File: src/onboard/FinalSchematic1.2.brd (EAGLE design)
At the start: 137.6 x 80 mm, 85 parts, among them IC1 MIC29310-5.0BT, IC3 A5975D

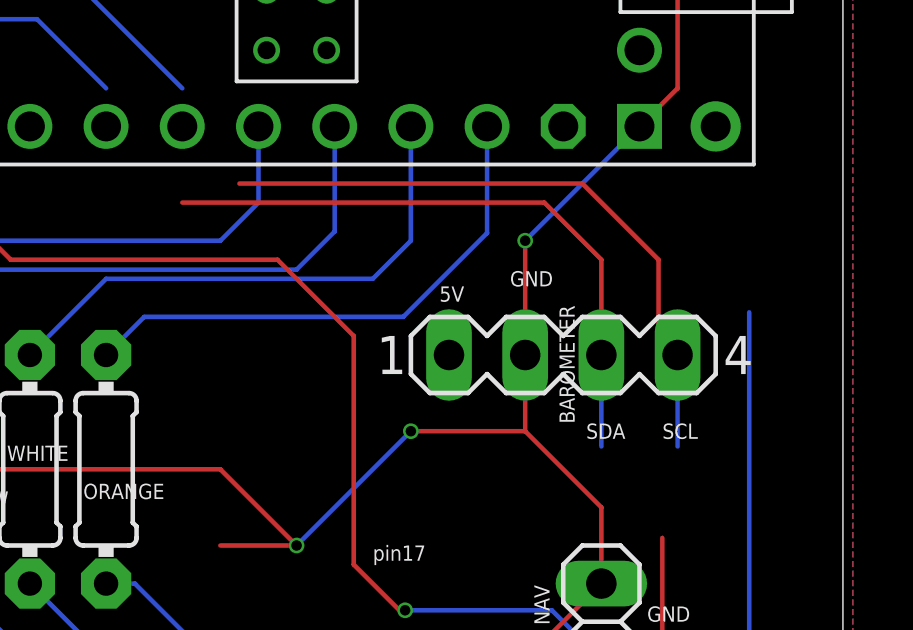
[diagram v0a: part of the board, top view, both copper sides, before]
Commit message: Removed old baro
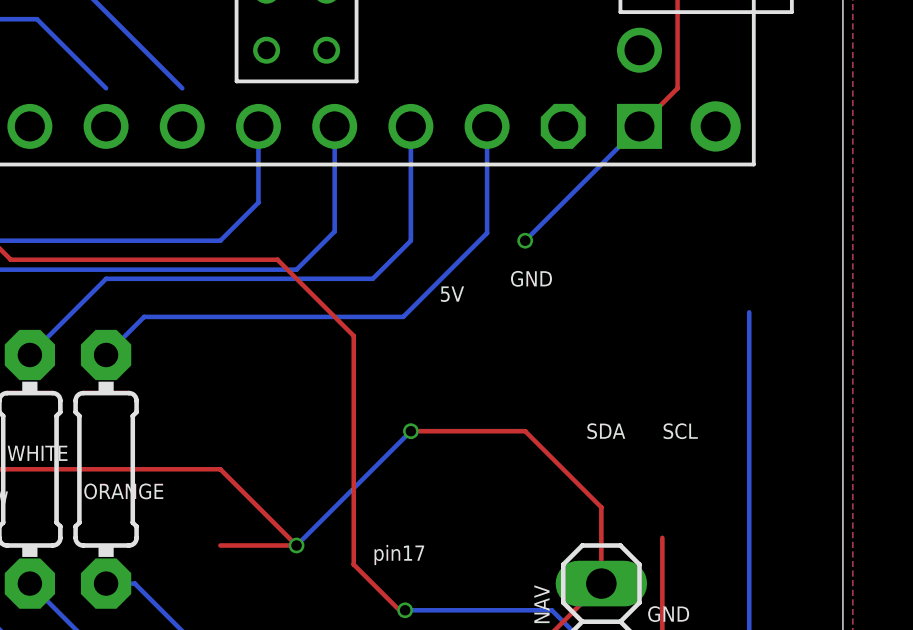
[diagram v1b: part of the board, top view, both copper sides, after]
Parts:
- removed BAROMETER: (no value), con-lstb:MA04-1
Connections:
- net 5V: no longer BAROMETER.1
- net GND: no longer BAROMETER.2
- net SCL: no longer BAROMETER.4
- net SDA: no longer BAROMETER.3
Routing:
- net SCL: track 141.5 -> 120.0 mm
- net SDA: track 130.1 -> 109.1 mm
- net GND: track 373.3 -> 366.9 mm
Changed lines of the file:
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@@
 </autorouter>
 <elements>
-<element name="BAROMETER" library="con-lstb" library_urn="urn:adsk.eagle:library:162" package="MA04-1" package3d_urn="urn:adsk.eagle:package:8337/1" value="" x="92.71" y="26.67" smashed="yes">
-<attribute name="MF" value="" x="125.73" y="-57.15" size="1.778" layer="27" display="off"/>
-<attribute name="MPN" value="" x="125.73" y="-57.15" size="1.778" layer="27" display="off"/>
-<attribute name="NAME" x="93.091" y="24.384" size="0.508" layer="25" ratio="10" rot="R90"/>
-<attribute name="OC_FARNELL" value="unknown" x="125.73" y="-57.15" size="1.778" layer="27" display="off"/>
-<attribute name="OC_NEWARK" value="unknown" x="125.73" y="-57.15" size="1.778" layer="27" display="off"/>
-<attribute name="POPULARITY" value="41" x="125.73" y="-57.15" size="1.778" layer="27" display="off"/>
-<attribute name="VALUE" x="93.345" y="28.321" size="1.27" layer="27" ratio="10"/>
-</element>
 <element name="BLUE" library="adafruit" library_urn="urn:adsk.eagle:library:420" package="0204/7" package3d_urn="urn:adsk.eagle:package:6240596/1" value="80" x="53.34" y="27.94" smashed="yes" rot="R270">
 <attribute name="NAME" x="52.832" y="26.9494" size="0.508" layer="25" ratio="12"/>
@@
 <contactref element="C10" pad="1"/>
 <contactref element="GREEN" pad="1"/>
-<contactref element="BAROMETER" pad="1"/>
 <contactref element="TEENSY4.1" pad="VIN"/>
 <contactref element="RADIO" pad="1"/>
@@
 <contactref element="C2" pad="1"/>
 <wire x1="97.79" y1="34.29" x2="88.9" y2="73.66" width="0" layer="19" extent="1-1"/>
-<wire x1="88.9" y1="26.67" x2="97.79" y2="34.29" width="0" layer="19" extent="1-1"/>
-<wire x1="68.58" y1="16.51" x2="88.9" y2="26.67" width="0" layer="19" extent="1-1"/>
+<wire x1="68.58" y1="16.51" x2="97.79" y2="34.29" width="0" layer="19" extent="1-1"/>
 <wire x1="64.77" y1="10.795" x2="68.58" y2="16.51" width="0" layer="19" extent="1-1"/>
 <wire x1="54.61" y1="19.05" x2="64.77" y2="10.795" width="0" layer="19" extent="1-1"/>
@@
 <contactref element="SERVO_DRIVER" pad="27"/>
 <contactref element="IMU" pad="SDA"/>
-<contactref element="BAROMETER" pad="3"/>
-<wire x1="93.98" y1="23.622" x2="93.98" y2="26.67" width="0.1524" layer="16"/>
 <wire x1="34.627" y1="39.156" x2="48.474" y2="39.156" width="0.1524" layer="16"/>
 <wire x1="48.474" y1="39.156" x2="49.7666" y2="37.8634" width="0.1524" layer="16"/>
@@
 <wire x1="49.7666" y1="37.8634" x2="75.1666" y2="37.8634" width="0.1524" layer="16"/>
 <contactref element="NAV" pad="3"/>
-<wire x1="93.98" y1="29.845" x2="93.98" y2="26.67" width="0.1524" layer="1"/>
 <wire x1="97.155" y1="13.97" x2="93.98" y2="13.97" width="0.1524" layer="16"/>
 <wire x1="97.79" y1="14.605" x2="97.155" y2="13.97" width="0.1524" layer="16"/>
@@
 <wire x1="33.143" y1="40.64" x2="34.627" y2="39.156" width="0.1524" layer="1"/>
 <via x="-10.16" y="40.64" extent="1-16" drill="0.35"/>
-<wire x1="93.98" y1="29.845" x2="92.075" y2="31.75" width="0.1524" layer="1"/>
-<wire x1="92.075" y1="31.75" x2="80.01" y2="31.75" width="0.1524" layer="1"/>
 <contactref element="TEENSY4.1" pad="18-A4/SDA0"/>
 <contactref element="R33" pad="1"/>
 <contactref element="TP2" pad="TP"/>
-<wire x1="77.47" y1="34.29" x2="80.01" y2="31.75" width="0" layer="19" extent="1-1"/>
 <wire x1="77.47" y1="35.56" x2="77.47" y2="34.29" width="0" layer="19" extent="16-16"/>
 <wire x1="-12.7" y1="38.1" x2="-10.16" y2="40.64" width="0" layer="19" extent="1-1"/>
-<wire x1="93.98" y1="13.97" x2="93.98" y2="23.622" width="0" layer="19" extent="16-16"/>
+<wire x1="93.98" y1="13.97" x2="77.47" y2="34.29" width="0" layer="19" extent="1-1"/>
 <wire x1="-34.544" y1="-70.612" x2="-24.365" y2="38.972" width="0" layer="19" extent="1-1"/>
 </signal>
@@
 <contactref element="SERVO_DRIVER" pad="26"/>
 <contactref element="IMU" pad="SCL"/>
-<contactref element="BAROMETER" pad="4"/>
 <wire x1="80.01" y1="35.56" x2="74.93" y2="40.64" width="0.1524" layer="16"/>
-<wire x1="96.52" y1="26.67" x2="96.52" y2="23.622" width="0.1524" layer="16"/>
 <wire x1="34.827" y1="41.656" x2="48.514" y2="41.656" width="0.1524" layer="16"/>
 <wire x1="48.514" y1="41.656" x2="49.53" y2="40.64" width="0.1524" layer="16"/>
@@
 <wire x1="32.287" y1="41.656" x2="32.033" y2="41.91" width="0.1524" layer="1"/>
 <wire x1="-12.7" y1="41.91" x2="32.033" y2="41.91" width="0.1524" layer="1"/>
-<wire x1="96.52" y1="26.67" x2="95.885" y2="27.305" width="0.1524" layer="1"/>
-<wire x1="95.885" y1="27.305" x2="95.885" y2="29.845" width="0.1524" layer="1"/>
-<wire x1="95.885" y1="29.845" x2="93.345" y2="32.385" width="0.1524" layer="1"/>
-<wire x1="93.345" y1="32.385" x2="81.915" y2="32.385" width="0.1524" layer="1"/>
 <contactref element="TEENSY4.1" pad="19-A5/SCL0"/>
 <contactref element="R32" pad="1"/>
 <contactref element="TP3" pad="TP"/>
-<wire x1="80.01" y1="34.29" x2="81.915" y2="32.385" width="0" layer="19" extent="1-1"/>
 <wire x1="80.01" y1="35.56" x2="80.01" y2="34.29" width="0" layer="19" extent="16-16"/>
-<wire x1="96.012" y1="20.574" x2="96.52" y2="23.622" width="0" layer="19" extent="1-16"/>
 <wire x1="-10.16" y1="45.72" x2="-12.7" y2="41.91" width="0" layer="19" extent="1-1"/>
+<wire x1="96.012" y1="20.574" x2="80.01" y2="34.29" width="0" layer="19" extent="1-1"/>
 <wire x1="-34.544" y1="-75.184" x2="-25.015" y2="38.972" width="0" layer="19" extent="1-1"/>
 </signal>
@@
 <contactref element="GPSMTK3339" pad="GND"/>
 <contactref element="RADIO" pad="2"/>
-<contactref element="BAROMETER" pad="2"/>
 <contactref element="SERVO_DRIVER" pad="25"/>
 <contactref element="C10" pad="2"/>
@@
 <contactref element="R53" pad="1"/>
 <contactref element="C12" pad="2"/>
-<wire x1="91.44" y1="26.67" x2="91.44" y2="30.48" width="0.1524" layer="1"/>
 <via x="91.44" y="30.48" extent="1-16" drill="0.35"/>
 <wire x1="95.25" y1="34.29" x2="91.44" y2="30.48" width="0.1524" layer="16"/>
@@
 <contactref element="NAV" pad="1"/>
 <wire x1="93.98" y1="21.59" x2="91.44" y2="24.13" width="0.1524" layer="1"/>
-<wire x1="91.44" y1="24.13" x2="91.44" y2="26.67" width="0.1524" layer="1"/>
 <wire x1="93.98" y1="21.59" x2="93.98" y2="19.05" width="0.1524" layer="1"/>
 <contactref element="C3" pad="2"/>
@@
 <wire x1="62.23" y1="34.29" x2="57.658" y2="29.464" width="0" layer="19" extent="1-1"/>
 <wire x1="76.2" y1="15.24" x2="81.28" y2="20.32" width="0" layer="19" extent="1-1"/>
+<wire x1="91.44" y1="30.48" x2="87.63" y2="24.13" width="0" layer="19" extent="1-1"/>
 <wire x1="52.07" y1="41.91" x2="62.23" y2="34.29" width="0" layer="19" extent="1-1"/>
 <wire x1="83.82" y1="46.53" x2="97.79" y2="49.53" width="0" layer="19" extent="1-1"/>

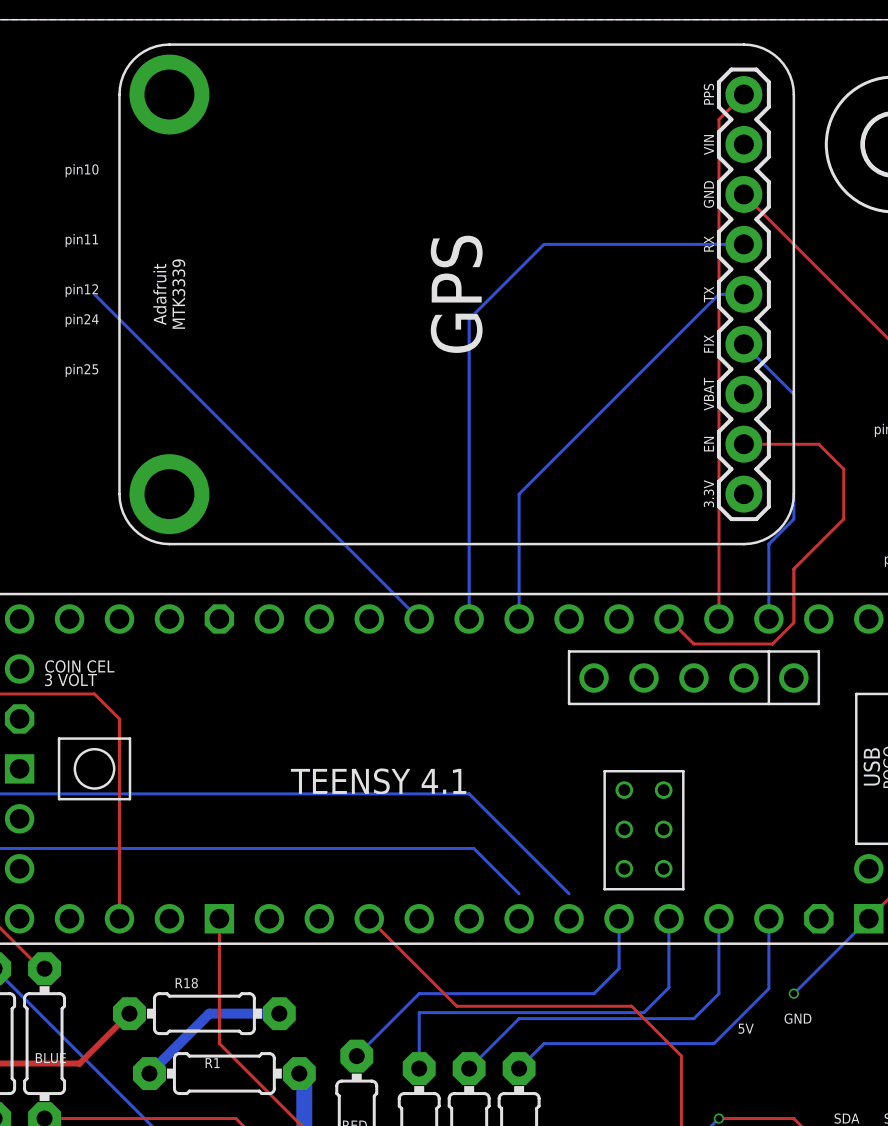
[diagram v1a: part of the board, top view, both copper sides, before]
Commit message: Rewired pins for easier routing
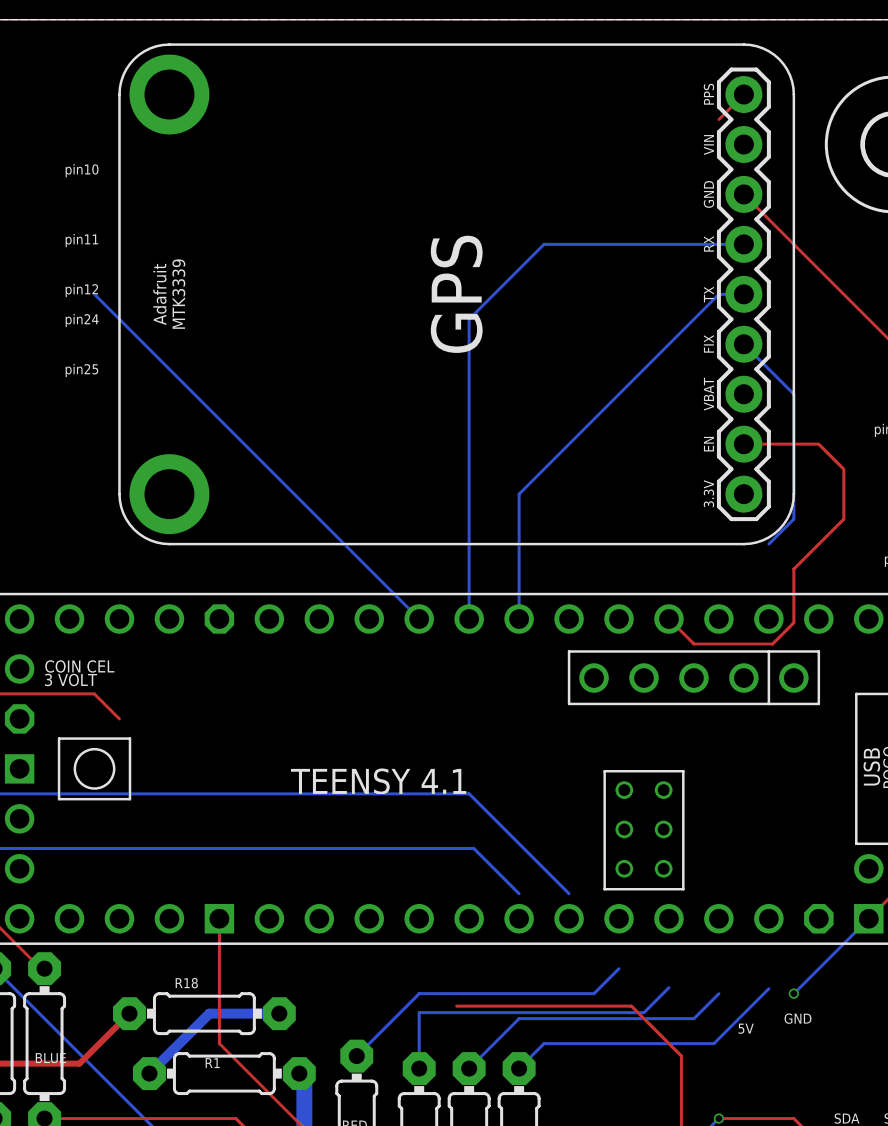
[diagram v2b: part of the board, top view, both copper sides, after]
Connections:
- net AUX_DATA: now also TEENSY4.1.6-OUT1D; no longer TEENSY4.1.9-OUT1C
- net BTN1: now also TEENSY4.1.14-A0/TX3/SPDIF_OUT
- net BTN2: now also TEENSY4.1.15-A1/RX3/SPDIF_IN
- net GPS_FIX: now also TEENSY4.1.3-LRCLK2; no longer TEENSY4.1.2-OUT2
- net GPS_PPS: now also TEENSY4.1.5-IN2; no longer TEENSY4.1.3-LRCLK2
- net IMU_INT: now also TEENSY4.1.22-A8/CTX1; no longer TEENSY4.1.40-A16/CS1
- net O_LED: now also TEENSY4.1.40-A16/CS1; no longer TEENSY4.1.23-A9/CRX1/MCLK1
- net RADIO_RST: now also TEENSY4.1.9-OUT1C; no longer TEENSY4.1.6-OUT1D
- net R_LED: now also TEENSY4.1.41-A17/MISO1; no longer TEENSY4.1.20-A6/TX5/LRCLK1
- net SELECT_PIN: now also TEENSY4.1.2-OUT2; no longer TEENSY4.1.15-A1/RX3/SPDIF_IN
- net W_LED: now also TEENSY4.1.38-A14/CS/IN1; no longer TEENSY4.1.22-A8/CTX1
- net Y_LED: now also TEENSY4.1.39-A15/CS/OUT1A; no longer TEENSY4.1.21-A7/RX5/BCLK1
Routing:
- net GPS_PPS: track 27.2 -> 1.80 mm
- net RADIO_RST: track 21.9 -> 45.2 mm
- net AUX_DATA: track 23.3 -> 0.00 mm
- net IMU_INT: track 33.9 -> 23.7 mm
- net SELECT_PIN: track 36.0 -> 29.7 mm
- net GPS_FIX: track 15.5 -> 11.7 mm
- net W_LED: track 18.1 -> 14.3 mm
- net O_LED: track 17.9 -> 14.4 mm
- net Y_LED: track 19.6 -> 16.1 mm
- net R_LED: track 17.7 -> 15.2 mm
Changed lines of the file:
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@@
 <signal name="GPS_FIX">
 <contactref element="GPSMTK3339" pad="FIX"/>
-<contactref element="TEENSY4.1" pad="2-OUT2"/>
 <wire x1="90.17" y1="53.34" x2="91.44" y2="54.61" width="0.1524" layer="16"/>
 <wire x1="91.44" y1="54.61" x2="91.44" y2="60.96" width="0.1524" layer="16"/>
 <wire x1="91.44" y1="60.96" x2="88.9" y2="63.5" width="0.1524" layer="16"/>
-<wire x1="90.17" y1="49.53" x2="90.17" y2="53.34" width="0.1524" layer="16"/>
+<contactref element="TEENSY4.1" pad="3-LRCLK2"/>
+<wire x1="87.63" y1="49.53" x2="90.17" y2="53.34" width="0" layer="19" extent="16-16"/>
 </signal>
 <signal name="GPS_PPS">
 <contactref element="GPSMTK3339" pad="PPS"/>
-<contactref element="TEENSY4.1" pad="3-LRCLK2"/>
-<wire x1="87.63" y1="49.53" x2="87.63" y2="74.93" width="0.1524" layer="1"/>
 <wire x1="87.63" y1="74.93" x2="88.9" y2="76.2" width="0.1524" layer="1"/>
+<contactref element="TEENSY4.1" pad="5-IN2"/>
+<wire x1="82.55" y1="49.53" x2="87.63" y2="74.93" width="0" layer="19" extent="1-1"/>
 </signal>
 <signal name="RADIO_EN">
@@
 <wire x1="44.45" y1="54.61" x2="44.45" y2="74.68" width="0.1524" layer="1"/>
 <wire x1="44.45" y1="74.68" x2="44.575" y2="74.805" width="0.1524" layer="1"/>
-<contactref element="TEENSY4.1" pad="6-OUT1D"/>
-<wire x1="44.45" y1="54.61" x2="80.01" y2="49.53" width="0" layer="19" extent="1-1"/>
+<contactref element="TEENSY4.1" pad="9-OUT1C"/>
+<wire x1="72.39" y1="49.53" x2="55.88" y2="66.04" width="0.1524" layer="16"/>
+<wire x1="45.72" y1="75.95" x2="55.88" y2="66.04" width="0" layer="19" extent="16-16"/>
 </signal>
 <signal name="RX2">
@@
 <signal name="IMU_INT">
 <contactref element="IMU" pad="INT"/>
-<contactref element="TEENSY4.1" pad="40-A16/CS1"/>
 <wire x1="36.191" y1="45.72" x2="34.627" y2="44.156" width="0.1524" layer="1"/>
 <wire x1="55.88" y1="45.72" x2="57.15" y2="44.45" width="0.1524" layer="1"/>
-<wire x1="57.15" y1="44.45" x2="57.15" y2="34.29" width="0.1524" layer="1"/>
 <wire x1="36.191" y1="45.72" x2="55.88" y2="45.72" width="0.1524" layer="1"/>
+<contactref element="TEENSY4.1" pad="22-A8/CTX1"/>
+<wire x1="57.15" y1="44.45" x2="87.63" y2="34.29" width="0" layer="19" extent="1-1"/>
 </signal>
 <signal name="RED">
@@
 <signal name="W_LED">
 <contactref element="WHITE" pad="1"/>
-<contactref element="TEENSY4.1" pad="22-A8/CTX1"/>
 <wire x1="87.63" y1="30.48" x2="86.36" y2="29.21" width="0.1524" layer="16"/>
-<wire x1="87.63" y1="30.48" x2="87.63" y2="34.29" width="0.1524" layer="16"/>
 <wire x1="77.47" y1="29.21" x2="74.93" y2="26.67" width="0.1524" layer="16"/>
 <wire x1="86.36" y1="29.21" x2="77.47" y2="29.21" width="0.1524" layer="16"/>
+<contactref element="TEENSY4.1" pad="38-A14/CS/IN1"/>
+<wire x1="52.07" y1="34.29" x2="74.93" y2="26.67" width="0" layer="19" extent="1-1"/>
 </signal>
 <signal name="Y_LED">
 <contactref element="YELLOW" pad="1"/>
-<contactref element="TEENSY4.1" pad="21-A7/RX5/BCLK1"/>
 <wire x1="85.09" y1="30.7848" x2="83.82" y2="29.5148" width="0.1524" layer="16"/>
-<wire x1="85.09" y1="30.7848" x2="85.09" y2="34.29" width="0.1524" layer="16"/>
 <wire x1="72.39" y1="29.5148" x2="72.39" y2="26.67" width="0.1524" layer="16"/>
 <wire x1="83.82" y1="29.5148" x2="72.39" y2="29.5148" width="0.1524" layer="16"/>
+<contactref element="TEENSY4.1" pad="39-A15/CS/OUT1A"/>
+<wire x1="54.61" y1="34.29" x2="72.39" y2="26.67" width="0" layer="19" extent="1-1"/>
 </signal>
 <signal name="R_LED">
 <contactref element="RED" pad="1"/>
-<contactref element="TEENSY4.1" pad="20-A6/TX5/LRCLK1"/>
 <wire x1="82.55" y1="31.75" x2="81.28" y2="30.48" width="0.1524" layer="16"/>
-<wire x1="82.55" y1="31.75" x2="82.55" y2="34.29" width="0.1524" layer="16"/>
 <wire x1="72.39" y1="30.48" x2="69.215" y2="27.305" width="0.1524" layer="16"/>
 <wire x1="81.28" y1="30.48" x2="72.39" y2="30.48" width="0.1524" layer="16"/>
+<contactref element="TEENSY4.1" pad="41-A17/MISO1"/>
+<wire x1="59.69" y1="34.29" x2="69.215" y2="27.305" width="0" layer="19" extent="1-1"/>
 </signal>
 <signal name="B_LED">
@@
 </signal>
 <signal name="AUX_DATA">
-<contactref element="TEENSY4.1" pad="9-OUT1C"/>
-<wire x1="72.39" y1="49.53" x2="55.88" y2="66.04" width="0.1524" layer="16"/>
+<contactref element="TEENSY4.1" pad="6-OUT1D"/>
 </signal>
 <signal name="SELECT_PIN">
 <contactref element="NAV" pad="2"/>
-<contactref element="TEENSY4.1" pad="15-A1/RX3/SPDIF_IN"/>
 <wire x1="87.249" y1="18.161" x2="85.725" y2="19.685" width="0.1524" layer="1"/>
 <wire x1="85.725" y1="19.685" x2="85.725" y2="27.305" width="0.1524" layer="1"/>
 <wire x1="85.725" y1="27.305" x2="83.185" y2="29.845" width="0.1524" layer="1"/>
 <wire x1="83.185" y1="29.845" x2="74.295" y2="29.845" width="0.1524" layer="1"/>
-<wire x1="74.295" y1="29.845" x2="69.85" y2="34.29" width="0.1524" layer="1"/>
 <via x="87.4381" y="18.161" extent="1-16" drill="0.35"/>
 <wire x1="87.4381" y1="18.161" x2="87.249" y2="18.161" width="0.1524" layer="1"/>
@@
 <wire x1="92.329" y1="18.161" x2="93.98" y2="16.51" width="0.1524" layer="16"/>
 <contactref element="R23" pad="2"/>
-<wire x1="87.4381" y1="18.161" x2="-27.178" y2="-110.236" width="0" layer="19" extent="1-1"/>
+<contactref element="TEENSY4.1" pad="2-OUT2"/>
+<wire x1="74.295" y1="29.845" x2="90.17" y2="49.53" width="0" layer="19" extent="1-1"/>
+<wire x1="-27.178" y1="-110.236" x2="87.4381" y2="18.161" width="0" layer="19" extent="1-1"/>
 </signal>
 <signal name="O_LED">
 <contactref element="ORANGE" pad="1"/>
-<contactref element="TEENSY4.1" pad="23-A9/CRX1/MCLK1"/>
-<wire x1="90.17" y1="34.29" x2="90.17" y2="30.734" width="0.1524" layer="16"/>
 <wire x1="87.376" y1="27.94" x2="78.74" y2="27.94" width="0.1524" layer="16"/>
 <wire x1="78.74" y1="27.94" x2="77.47" y2="26.67" width="0.1524" layer="16"/>
 <wire x1="90.17" y1="30.734" x2="87.376" y2="27.94" width="0.1524" layer="16"/>
+<contactref element="TEENSY4.1" pad="40-A16/CS1"/>
+<wire x1="57.15" y1="34.29" x2="77.47" y2="26.67" width="0" layer="19" extent="1-1"/>
 </signal>
 <signal name="ORANGE">
@@
 <contactref element="BTNBANK" pad="1"/>
 <contactref element="TEENSY4.1" pad="25-A11/RX6/SDA2"/>
+<contactref element="TEENSY4.1" pad="15-A1/RX3/SPDIF_IN"/>
+<wire x1="69.85" y1="34.29" x2="57.15" y2="49.53" width="0" layer="19" extent="1-1"/>
 <wire x1="-27.178" y1="-22.86" x2="57.15" y2="49.53" width="0" layer="19" extent="1-1"/>
 <wire x1="-33.528" y1="-39.116" x2="-27.178" y2="-22.86" width="0" layer="19" extent="1-1"/>
@@
 <contactref element="BTNBANK" pad="2"/>
 <contactref element="TEENSY4.1" pad="24-A10/TX6/SCL2"/>
-<wire x1="-27.178" y1="-18.796" x2="59.69" y2="49.53" width="0" layer="19" extent="1-1"/>
+<contactref element="TEENSY4.1" pad="14-A0/TX3/SPDIF_OUT"/>
+<wire x1="67.31" y1="34.29" x2="59.69" y2="49.53" width="0" layer="19" extent="1-1"/>
+<wire x1="-27.178" y1="-18.796" x2="67.31" y2="34.29" width="0" layer="19" extent="1-1"/>
 <wire x1="-30.988" y1="-39.116" x2="-27.178" y2="-18.796" width="0" layer="19" extent="1-1"/>
 </signal>
